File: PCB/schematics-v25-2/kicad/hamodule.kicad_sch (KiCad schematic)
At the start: 189 parts, among them J1 GND|5V, J10 Tx|Rx, J11 Sda|Scl, J12 3|9, J13 13|12, J14 3.3v|GND|7|15, J15 2604-1104, J16 2604-1104, J17 TestPoint, J19 TestPoint, J2 2604-1102, J3 USB_C_Receptacle_USB2.0, J4 GND|3.3V, J5 Conn_01x02_Pin, J6 2604-1104, J7 2604-1104, J8 5v|GND|Do, J9 Screen, K1 AQG22205, K2 AQG22205, K3 AQG22205, K4 AQG22205, K5 AQG22205, K6 AQG22205, K7 AQG22205, K8 AQG22205, SW1 USB | PS, SW2 Reset, SW3 Boot, U1 LD1117AV33, U10 SN74LV1T34DBV, U11 ULN2803A, U12 TCAL6416, U14 74AHC1G04, U2 USBLC6-2SC6, U3 ESP32-S3-WROOM-2, U4 LDA210, U5 LDA210, U6 LDA210, U7 LDA210, U8 SHT4x, U9 SN74LVCH8T245

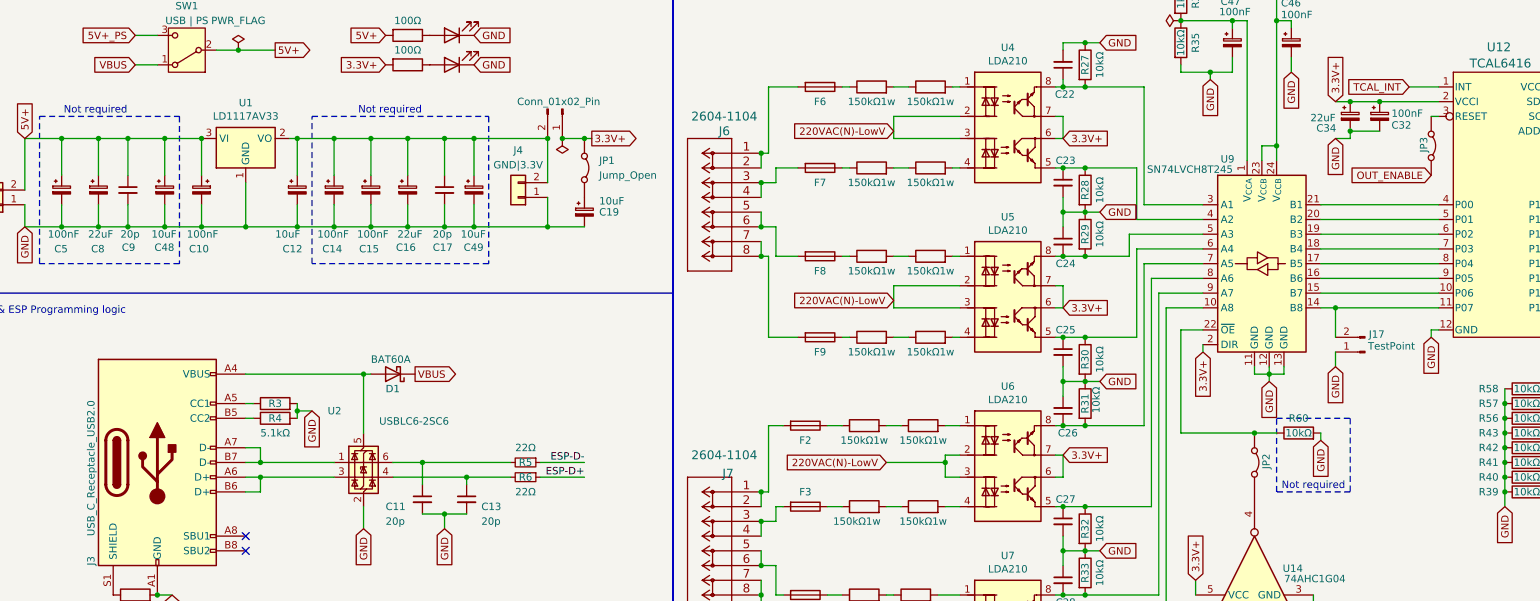
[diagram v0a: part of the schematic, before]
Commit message: Moving ICs to the top
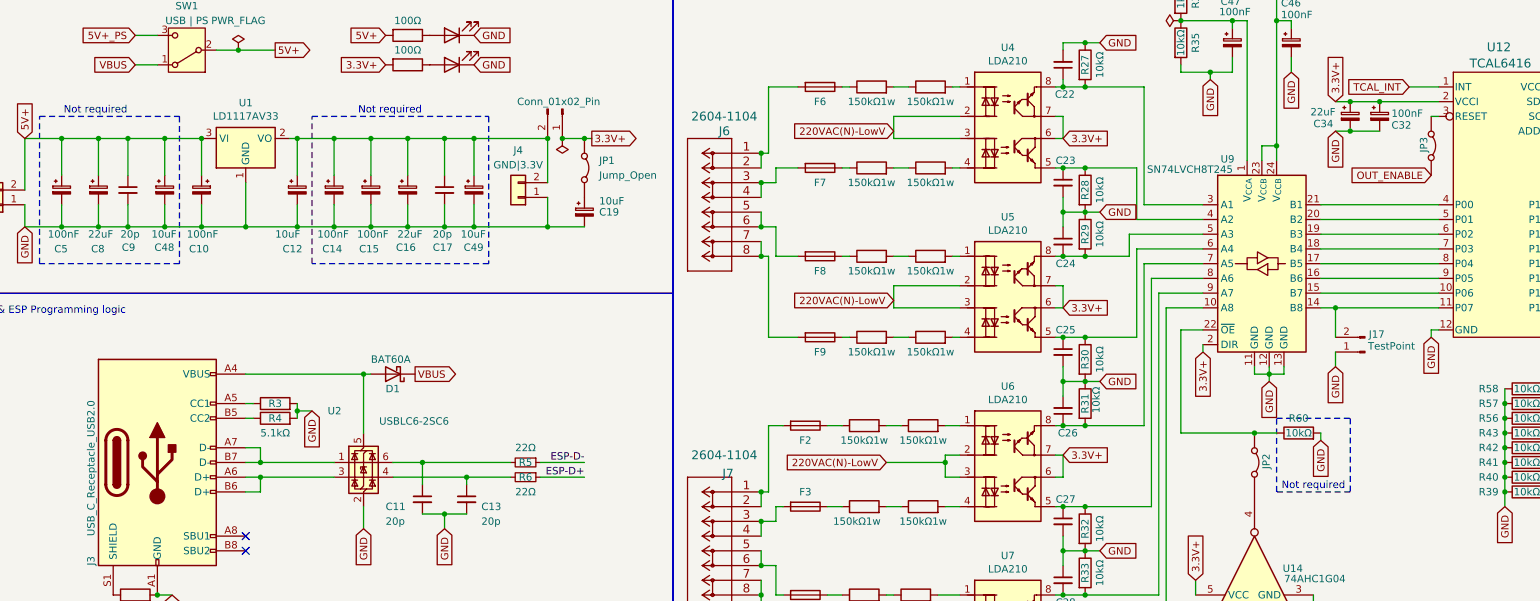
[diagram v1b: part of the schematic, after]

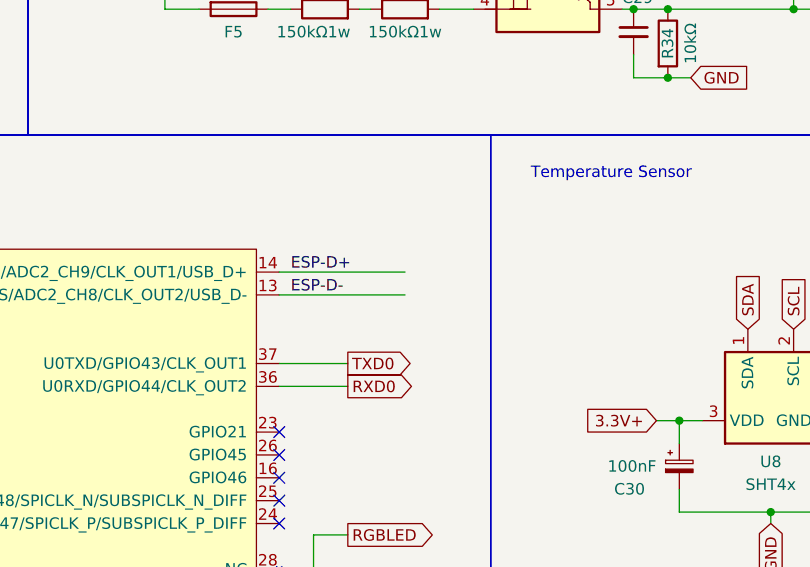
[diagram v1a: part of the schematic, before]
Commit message: fixing issue caused by Kicad8. Kicad 9 with many ERC fixed
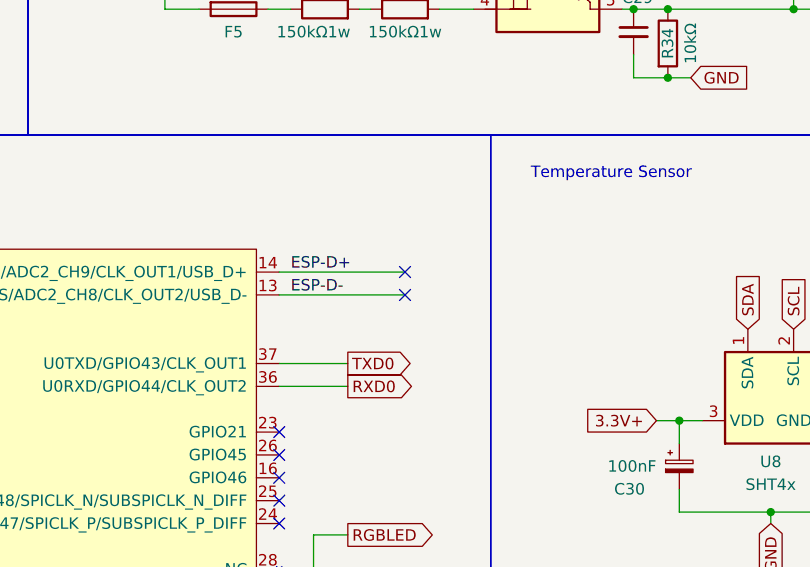
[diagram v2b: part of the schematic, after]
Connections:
- no-connect marks 34 -> 36
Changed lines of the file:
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@@
 	)
 	(no_connect
+		(at 176.53 199.39)
+	)
+	(no_connect
 		(at 44.45 218.44)
 	)
@@
 	)
 	(no_connect
+		(at 176.53 201.93)
+	)
+	(no_connect
 		(at 276.86 279.4)
 	)
@@
 			)
 		)
-		(property "Sim.Library" "${KICAD7_SYMBOL_DIR}/Simulation_SPICE.sp"
+		(property "Sim.Library" "${KICAD9_SYMBOL_DIR}/Simulation_SPICE.sp"
 			(at 58.42 36.83 0)
 			(effects
@@
 		)
 		(property "Footprint" "wago-2604-1104:big_pads_2604-1104"
-			(at 139.7 144.526 0)
+			(at 140.97 133.35 0)
 			(effects
 				(font
@@
 			)
 		)
-		(property "PcbText" ""
-			(at 139.7 146.05 0)
-			(effects
-				(font
-					(size 1.27 1.27)
-				)
-			)
-		)
-		(property "Field4" ""
-			(at 139.7 146.05 0)
-			(effects
-				(font
-					(size 1.27 1.27)
-				)
-				(hide yes)
-			)
-		)
 		(pin "1"
 		)
@@
 		)
 		(property "Footprint" "wago-2604-1104:big_pads_2604-1104"
-			(at 403.86 92.964 0)
+			(at 402.59 104.14 0)
 			(effects
 				(font
@@
 			)
 		)
-		(property "PcbText" ""
-			(at 403.86 91.44 0)
-			(effects
-				(font
-					(size 1.27 1.27)
-				)
-			)
-		)
-		(property "Field4" ""
-			(at 403.86 91.44 0)
-			(effects
-				(font
-					(size 1.27 1.27)
-				)
-				(hide yes)
-			)
-		)
 		(pin "1"
 		)
@@
 					(size 1.27 1.27)
 				)
+				(hide yes)
 			)
 		)
@@
 			)
 		)
+		(property "Sim.Pins" "1=K 2=A"
+			(at 96.52 59.69 0)
+			(effects
+				(font
+					(size 1.27 1.27)
+				)
+				(hide yes)
+			)
+		)
 		(pin "1"
 		)
@@
 		)
 		(property "Footprint" "wago-2604-1104:big_pads_2604-1104"
-			(at 403.86 147.574 0)
+			(at 402.59 158.75 0)
 			(effects
 				(font
@@
 			)
 		)
-		(property "PcbText" ""
-			(at 403.86 146.05 0)
-			(effects
-				(font
-					(size 1.27 1.27)
-				)
-			)
-		)
-		(property "Field4" ""
-			(at 403.86 146.05 0)
-			(effects
-				(font
-					(size 1.27 1.27)
-				)
-				(hide yes)
-			)
-		)
 		(pin "1"
 		)
@@
 			)
 		)
+		(property "Sim.Pins" "1=K 2=A"
+			(at 273.05 275.59 0)
+			(effects
+				(font
+					(size 1.27 1.27)
+				)
+				(hide yes)
+			)
+		)
 		(pin "1"
 		)
@@
 			)
 		)
+		(property "Sim.Pins" "1=K 2=A"
+			(at 321.31 135.89 0)
+			(effects
+				(font
+					(size 1.27 1.27)
+				)
+				(hide yes)
+			)
+		)
+		(property "PcbText" ""
+			(at 321.31 135.89 0)
+			(effects
+				(font
+					(size 1.27 1.27)
+				)
+			)
+		)
 		(pin "1"
 		)
@@
 			)
 		)
+		(property "Sim.Pins" "1=K 2=A"
+			(at 321.31 123.19 0)
+			(effects
+				(font
+					(size 1.27 1.27)
+				)
+				(hide yes)
+			)
+		)
+		(property "PcbText" ""
+			(at 321.31 123.19 0)
+			(effects
+				(font
+					(size 1.27 1.27)
+				)
+			)
+		)
 		(pin "1"
 		)
@@
 			)
 		)
+		(property "Sim.Pins" "1=K 2=A"
+			(at 321.31 133.35 0)
+			(effects
+				(font
+					(size 1.27 1.27)
+				)
+				(hide yes)
+			)
+		)
+		(property "PcbText" ""
+			(at 321.31 133.35 0)
+			(effects
+				(font
+					(size 1.27 1.27)
+				)
+			)
+		)
 		(pin "1"
 		)
@@
 		)
 		(property "Footprint" "wago-2604-1104:big_pads_2604-1104"
-			(at 139.7 86.106 0)
+			(at 140.97 74.93 0)
 			(effects
 				(font
@@
 			)
 		)
-		(property "PcbText" ""
-			(at 139.7 87.63 0)
-			(effects
-				(font
-					(size 1.27 1.27)
-				)
-			)
-		)
-		(property "Field4" ""
-			(at 139.7 87.63 0)
-			(effects
-				(font
-					(size 1.27 1.27)
-				)
-				(hide yes)
-			)
-		)
 		(pin "1"
 		)
@@
 			)
 		)
+		(property "Sim.Pins" "1=K 2=A"
+			(at 269.24 275.59 0)
+			(effects
+				(font
+					(size 1.27 1.27)
+				)
+				(hide yes)
+			)
+		)
 		(pin "1"
 		)
@@
 					(size 1.27 1.27)
 				)
+				(hide yes)
 			)
 		)
@@
 			)
 		)
+		(property "Sim.Pins" "1=K 2=A"
+			(at 321.31 128.27 0)
+			(effects
+				(font
+					(size 1.27 1.27)
+				)
+				(hide yes)
+			)
+		)
 		(pin "1"
 		)
@@
 			)
 		)
+		(property "Sim.Pins" "1=K 2=A"
+			(at 321.31 138.43 0)
+			(effects
+				(font
+					(size 1.27 1.27)
+				)
+				(hide yes)
+			)
+		)
+		(property "PcbText" ""
+			(at 321.31 138.43 0)
+			(effects
+				(font
+					(size 1.27 1.27)
+				)
+			)
+		)
 		(pin "1"
 		)
@@
 			)
 		)
+		(property "Sim.Pins" "1=K 2=A"
+			(at 321.31 130.81 0)
+			(effects
+				(font
+					(size 1.27 1.27)
+				)
+				(hide yes)
+			)
+		)
+		(property "PcbText" ""
+			(at 321.31 130.81 0)
+			(effects
+				(font
+					(size 1.27 1.27)
+				)
+			)
+		)
 		(pin "1"
 		)
@@
 			)
 		)
+		(property "Sim.Pins" "1=K 2=A"
+			(at 364.49 244.856 0)
+			(effects
+				(font
+					(size 1.27 1.27)
+				)
+				(hide yes)
+			)
+		)
+		(property "PcbText" ""
+			(at 364.49 241.3 0)
+			(effects
+				(font
+					(size 1.27 1.27)
+				)
+			)
+		)
 		(pin "1"
 		)
@@
 					(size 1.27 1.27)
 				)
+				(hide yes)
 			)
 		)
@@
 			)
 		)
+		(property "Sim.Pins" "1=K 2=A"
+			(at 96.52 64.77 0)
+			(effects
+				(font
+					(size 1.27 1.27)
+				)
+				(hide yes)
+			)
+		)
 		(pin "1"
 		)
@@
 			)
 		)
+		(property "Sim.Pins" "1=K 2=A"
+			(at 321.31 120.65 0)
+			(effects
+				(font
+					(size 1.27 1.27)
+				)
+				(hide yes)
+			)
+		)
+		(property "PcbText" ""
+			(at 321.31 120.65 0)
+			(effects
+				(font
+					(size 1.27 1.27)
+				)
+			)
+		)
 		(pin "1"
 		)
@@
 			)
 		)
+		(property "Sim.Pins" "1=K 2=A"
+			(at 321.31 125.73 0)
+			(effects
+				(font
+					(size 1.27 1.27)
+				)
+				(hide yes)
+			)
+		)
+		(property "PcbText" ""
+			(at 321.31 125.73 0)
+			(effects
+				(font
+					(size 1.27 1.27)
+				)
+			)
+		)
 		(pin "1"
 		)
@@
 			)
 		)
-		(property "Datasheet" "https://www.ti.com/lit/ds/symlink/sn74lvch8t245.pdf"
+		(property "Datasheet" "https://www.ti.com/lit/ds/symlink/sn74lvch8t245.pd"
 			(at 235.966 129.032 0)
 			(effects

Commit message: pull-up for TCAL. Fix ERC. Fix 3D models. Fix Silkscreen
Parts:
- added R61: 10kΩ, Resistor_SMD:R_0603_1608Metric_Pad0.98x0.95mm_HandSolder, symbol Device:R
- C10, C14, C15, C16, C20, C21, C3, C30, C31, C32, C33, C34, C35, C36, C37, C38, C4, C40, C41, C46, C47, C48, C49, C5, C6, C7, C8: symbol Device:C_Polarized_Small -> Device:C_Small
- JP1, JP2, JP3: symbol Jumper:Jumper_2_Bridged -> Jumper:SolderJumper_2_Bridged; now left out of the parts list
- U8: footprint Sensor_Humidity:Sensirion_DFN-4_1.5x1.5mm_P0.8mm_SHT4x_NoCentralPad -> sht40:XDCR_SHT40-AD1B-R2
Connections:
- net 3.3V+: now also R61.1
- net at JP3.1 (A), U12.3 (RESET): now also R61.2
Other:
- moved on the sheet: R35, R36, R39, R40, R41, R42, R43, R56, R57, R58

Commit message: Adding GND vias close to signal. Separate signal vias to make sure that they dont create a large cut in layer 2 and 3. For example for the LEDs going to ULN or the R56, R57, etc. Their vias are not aligned anymore allowing copper between them in layers 2 and 3. Check the videos from Rick Hartley - How to achieve proper grounding and from Hans Rosenberg: Flawless PCB design Part 2
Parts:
- C1, C2, C43, C44: symbol Device:C_Polarized_Small -> Device:C_Small
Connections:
- no-connect marks 36 -> 34
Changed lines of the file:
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@@
 	)
 	(no_connect
-		(at 176.53 199.39)
-	)
-	(no_connect
 		(at 44.45 218.44)
 	)
@@
 	)
 	(no_connect
-		(at 176.53 201.93)
-	)
-	(no_connect
 		(at 276.86 279.4)
 	)
@@
 	(wire
 		(pts
-			(xy 162.56 201.93) (xy 176.53 201.93)
-		)
-		(stroke
-			(width 0)
-			(type default)
-		)
-	)
-	(wire
-		(pts
 			(xy 88.9 77.47) (xy 95.25 77.47)
 		)
@@
 		)
 	)
-	(polyline
-		(pts
-			(xy 401.32 147.32) (xy 400.05 147.32)
-		)
-		(stroke
-			(width 0)
-			(type default)
-		)
-	)
 	(wire
 		(pts
@@
 	(wire
 		(pts
+			(xy 162.56 199.39) (xy 166.37 199.39)
+		)
+		(stroke
+			(width 0)
+			(type default)
+		)
+	)
+	(wire
+		(pts
 			(xy 326.39 133.35) (xy 326.39 135.89)
 		)
@@
 	(wire
 		(pts
-			(xy 162.56 199.39) (xy 176.53 199.39)
-		)
-		(stroke
-			(width 0)
-			(type default)
-		)
-	)
-	(wire
-		(pts
 			(xy 322.58 130.81) (xy 326.39 130.81)
 		)
@@
 	(wire
 		(pts
+			(xy 162.56 201.93) (xy 166.37 201.93)
+		)
+		(stroke
+			(width 0)
+			(type default)
+		)
+	)
+	(wire
+		(pts
 			(xy 46.99 88.9) (xy 46.99 92.71)
 		)
@@
 	)
 	(label "ESP-D+"
-		(at 163.83 199.39 0)
+		(at 166.37 199.39 0)
 		(effects
 			(font
@@
 	)
 	(label "ESP-D-"
-		(at 163.83 201.93 0)
+		(at 166.37 201.93 0)
 		(effects
 			(font
@@
 	)
 	(symbol
+		(lib_name "2604-1104_2")
 		(lib_id "wago-2604-1104:2604-1104")
 		(at 403.86 91.44 0)
@@
 	)
 	(symbol
-		(lib_id "Device:C_Polarized_Small")
+		(lib_id "Device:C_Small")
 		(at 22.86 264.16 0)
 		(unit 1)
@@
 			)
 		)
-		(property "Description" "Polarized capacitor, small symbol"
+		(property "Description" "Unpolarized capacitor, small symbol"
 			(at 22.86 264.16 0)
 			(effects
@@
 	)
 	(symbol
+		(lib_name "2604-1104_1")
 		(lib_id "wago-2604-1104:2604-1104")
 		(at 403.86 146.05 0)
@@
 	)
 	(symbol
+		(lib_name "2604-1104_3")
 		(lib_id "wago-2604-1104:2604-1104")
 		(at 139.7 87.63 180)
@@
 	)
 	(symbol
-		(lib_id "Device:C_Polarized_Small")
+		(lib_id "Device:C_Small")
 		(at 41.91 264.16 0)
 		(unit 1)
@@
 			)
 		)
-		(property "Description" "Polarized capacitor, small symbol"
+		(property "Description" "Unpolarized capacitor, small symbol"
 			(at 41.91 264.16 0)
 			(effects
@@
 	)
 	(symbol
-		(lib_id "Device:C_Polarized_Small")
+		(lib_id "Device:C_Small")
 		(at 19.05 264.16 0)
 		(unit 1)
@@
 			)
 		)
-		(property "Description" "Polarized capacitor, small symbol"
+		(property "Description" "Unpolarized capacitor, small symbol"
 			(at 19.05 264.16 0)
 			(effects
@@
 	)
 	(symbol
-		(lib_id "Device:C_Polarized_Small")
+		(lib_id "Device:C_Small")
 		(at 38.1 264.16 0)
 		(unit 1)
@@
 			)
 		)
-		(property "Description" "Polarized capacitor, small symbol"
+		(property "Description" "Unpolarized capacitor, small symbol"
 			(at 38.1 264.16 0)
 			(effects

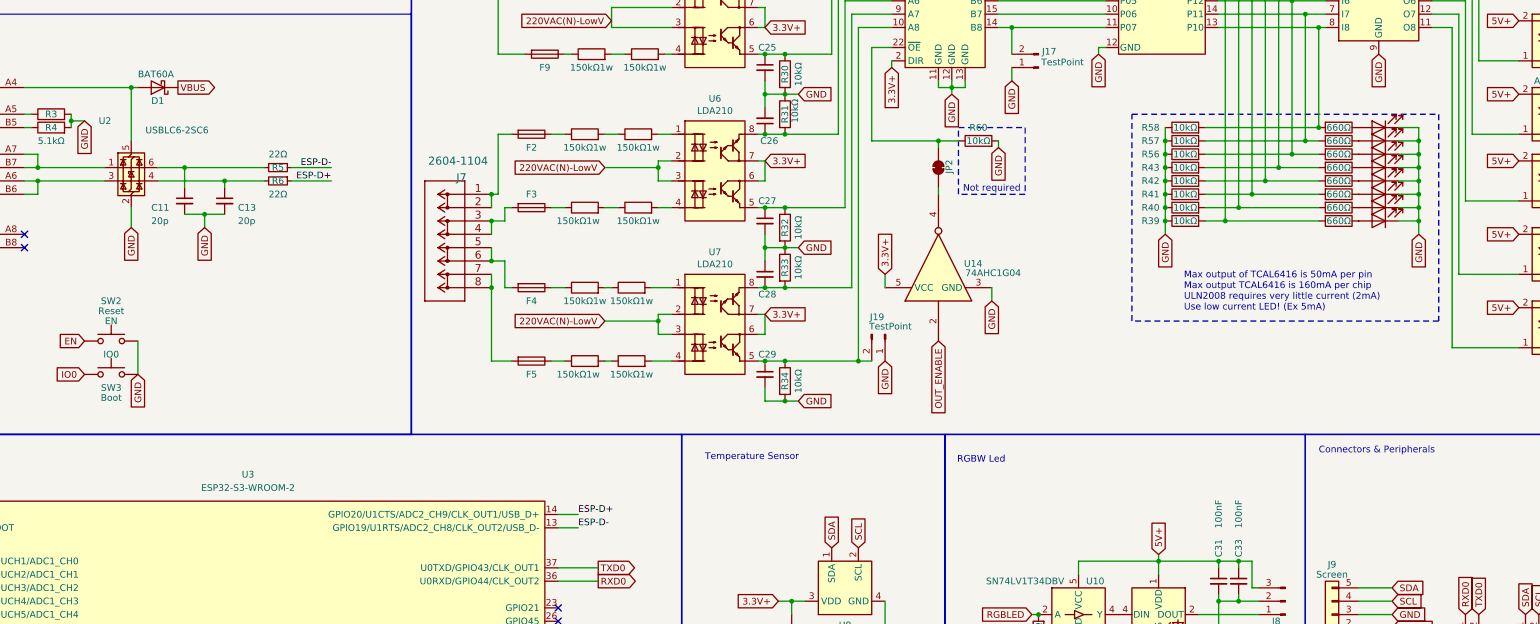
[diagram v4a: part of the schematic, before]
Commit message: Changes in the schematic look: 1. Align label text to the right, in order the trace is under the label. 2. Display resistors values for the resistors next to the LED (R45... R5x) 3. Align the identifier text for USB protection diodes
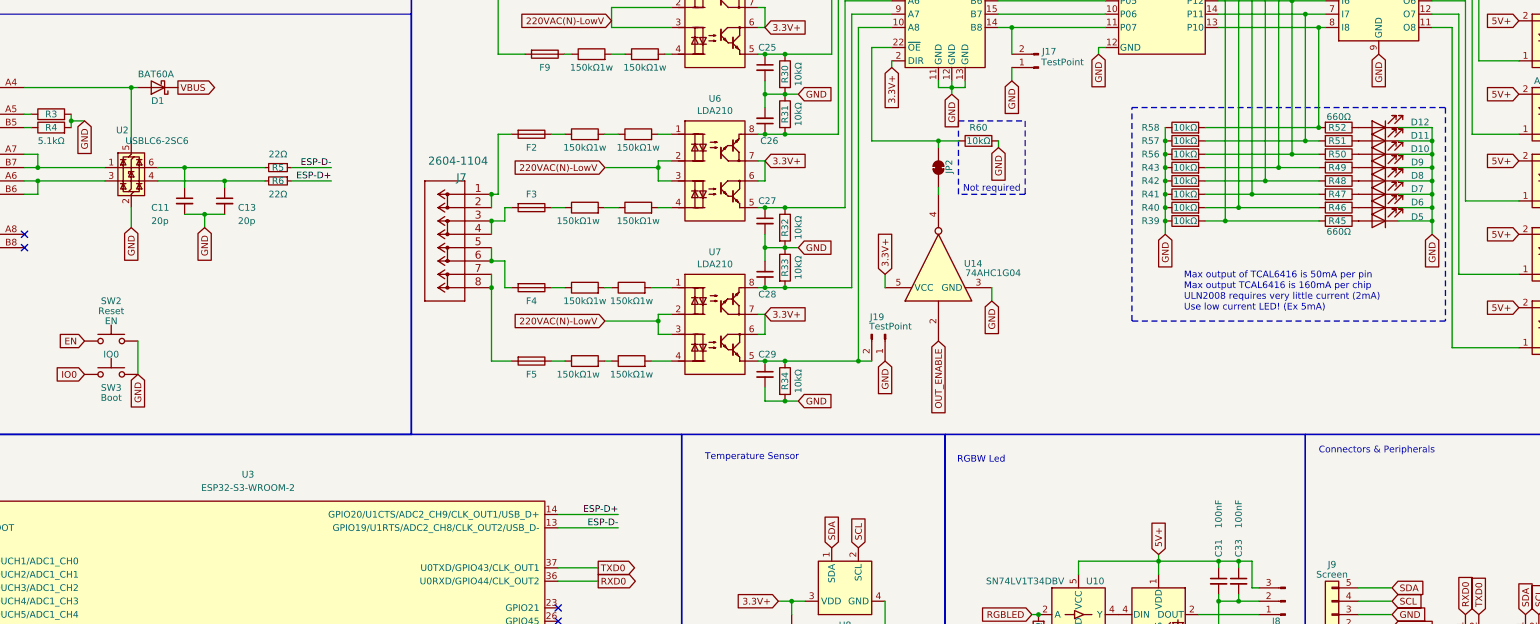
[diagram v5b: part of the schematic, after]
